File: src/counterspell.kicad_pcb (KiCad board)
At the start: 2 copper layers, 50.7 x 116.8 mm, 10 parts, among them SW1 SW_Push

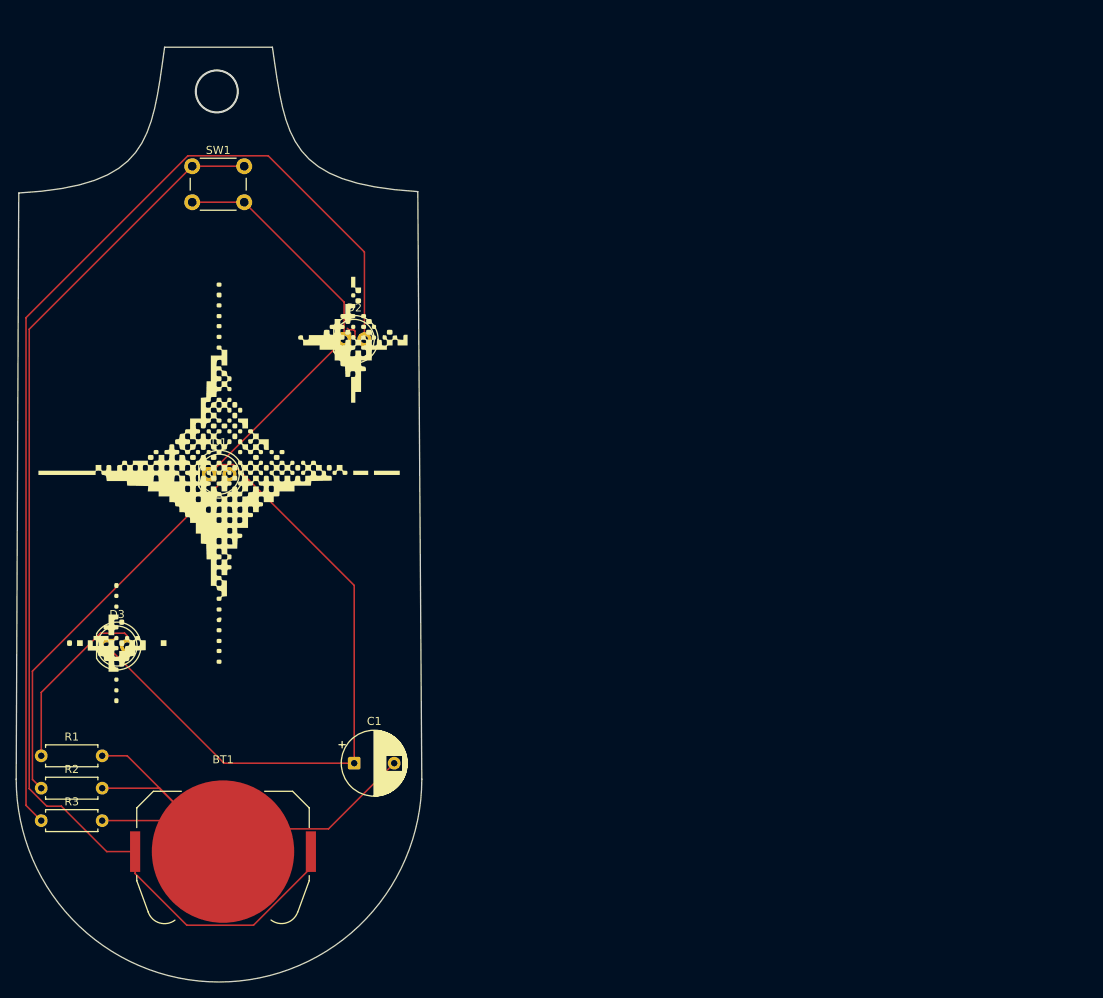
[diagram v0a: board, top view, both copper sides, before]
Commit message: perfect changed the whole board outlook like resized it
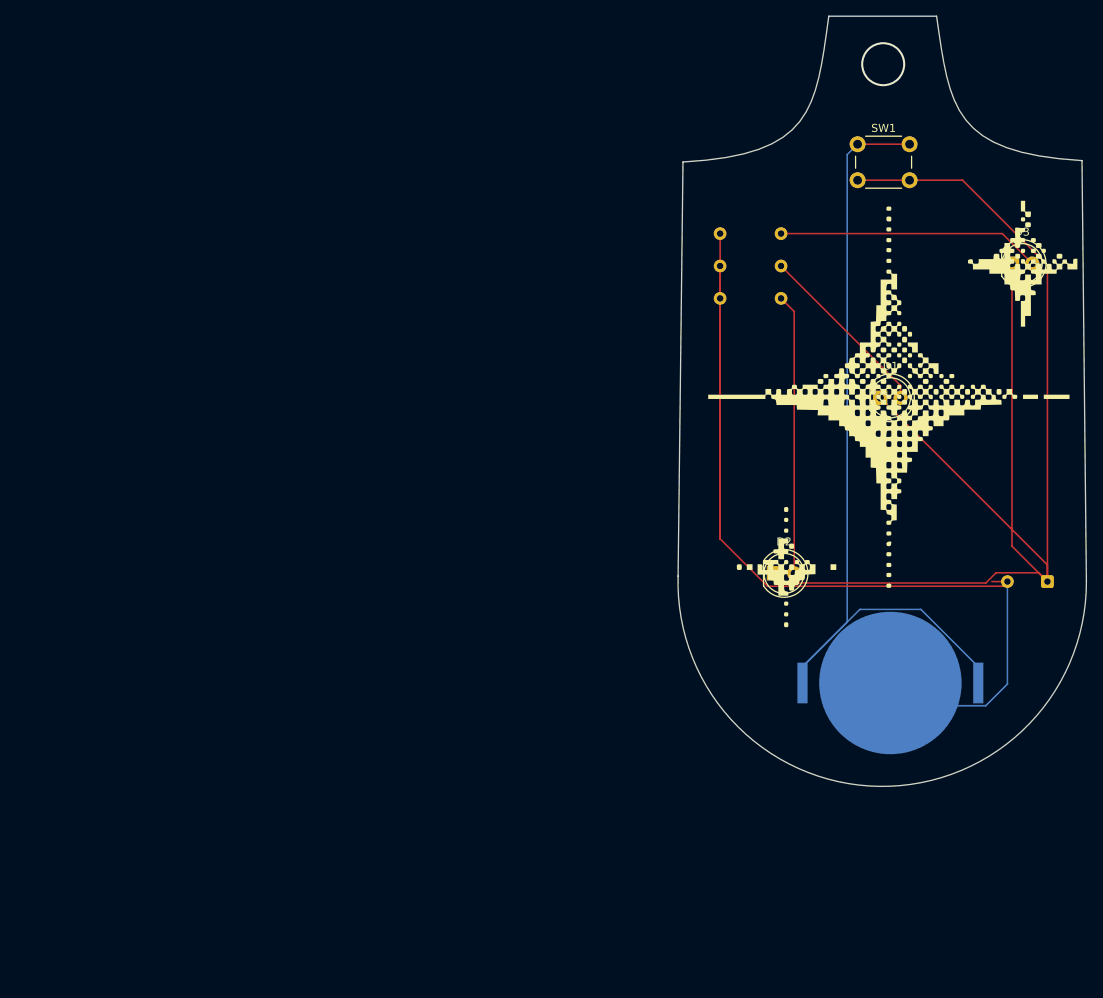
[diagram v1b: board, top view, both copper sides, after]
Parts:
- BT1, C1, R1, R2, R3: moved to B.Cu
- moved D3 122.8 mm to (249.8, 56.3)
- moved R1 113.2 mm to (220.9, 52.5), turned to 180 degrees
- moved R2 113.2 mm to (220.9, 56.6), turned to 180 degrees
- moved R3 113.2 mm to (220.9, 60.6), turned to 180 degrees
- moved C1 89.6 mm to (254.2, 96.0), turned to 180 degrees
- moved BT1 86.0 mm to (234.6, 108.7), turned to 180 degrees
- moved D1 84.4 mm to (233.3, 73.1)
- moved G*** 84.3 mm to (234.9, 75.1)
- moved SW1 83.2 mm to (230.5, 41.4)
- moved D2 61.2 mm to (220.0, 95.0)
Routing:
- net Net-(D2-A): track 130.2 -> 35.1 mm
- net Net-(BT1--): track 81.1 -> 172.6 mm
- net Net-(D1-K): track 138.5 -> 176.6 mm
- net Net-(BT1-+): track 141.6 -> 106.6 mm
- net Net-(D1-A): track 49.9 -> 22.7 mm
- net Net-(D3-A): track 23.1 -> 33.0 mm
- net (no net): track 1.87 -> 0.00 mm
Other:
- board size 50.7 x 116.8 mm -> 51 x 96.3 mm

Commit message: Update counterspell.kicad_pcb
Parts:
- added G***: LOGO, LOGO, B.Cu at (252.1, 81.3)
- added G***: LOGO, LOGO, B.Cu at (242.6, 75.6)

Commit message: important
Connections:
- C1 pad 1: Net-(D1-K) -> Net-(D1-A)
- D2 pad 1: Net-(D1-K) -> Net-(D2-K)
- D2 pad 2: Net-(D2-A) -> Net-(D1-A)
- D3 pad 1: Net-(D1-K) -> Net-(D3-K)
- D3 pad 2: Net-(D3-A) -> Net-(D1-A)
- R1 pad 1: Net-(D3-A) -> Net-(D3-K)
- R2 pad 1: Net-(D1-A) -> Net-(D1-K)
- R3 pad 1: Net-(D2-A) -> Net-(D2-K)
- SW1 pad 2: Net-(D1-K) -> Net-(D1-A)
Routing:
- net Net-(D1-K): track 176.6 -> 21.6 mm
- net Net-(D1-A): track 22.7 -> 107.8 mm
- net Net-(BT1--): track 172.6 -> 106.2 mm
- net Net-(D2-A): track 35.1 -> 0.00 mm
- net Net-(D2-K): track 0.00 -> 34.7 mm
- net Net-(D3-A): track 33.0 -> 0.00 mm
- net Net-(D3-K): track 0.00 -> 30.4 mm
- net Net-(BT1-+): track 106.6 -> 105.3 mm
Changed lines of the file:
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@@
 	(net 3 "Net-(D1-K)")
 	(net 4 "Net-(D1-A)")
-	(net 5 "Net-(D2-A)")
-	(net 6 "Net-(D3-A)")
+	(net 5 "Net-(D2-K)")
+	(net 6 "Net-(D3-K)")
 	(footprint "LED_THT:LED_D5.0mm"
 		(layer "F.Cu")
@@
 			(layers "*.Cu" "*.Mask")
 			(remove_unused_layers no)
-			(net 3 "Net-(D1-K)")
+			(net 6 "Net-(D3-K)")
 			(pinfunction "K")
 			(pintype "passive")
@@
 			(layers "*.Cu" "*.Mask")
 			(remove_unused_layers no)
-			(net 6 "Net-(D3-A)")
+			(net 4 "Net-(D1-A)")
 			(pinfunction "A")
 			(pintype "passive")
@@
 			(layers "*.Cu" "*.Mask")
 			(remove_unused_layers no)
-			(net 3 "Net-(D1-K)")
+			(net 5 "Net-(D2-K)")
 			(pinfunction "K")
 			(pintype "passive")
@@
 			(layers "*.Cu" "*.Mask")
 			(remove_unused_layers no)
-			(net 5 "Net-(D2-A)")
+			(net 4 "Net-(D1-A)")
 			(pinfunction "A")
 			(pintype "passive")
@@
 			(layers "*.Cu" "*.Mask")
 			(remove_unused_layers no)
-			(net 3 "Net-(D1-K)")
+			(net 4 "Net-(D1-A)")
 			(pinfunction "2")
 			(pintype "passive")
@@
 			(layers "*.Cu" "*.Mask")
 			(remove_unused_layers no)
-			(net 3 "Net-(D1-K)")
+			(net 4 "Net-(D1-A)")
 			(pinfunction "2")
 			(pintype "passive")
@@
 			(remove_unused_layers no)
 			(roundrect_rratio 0.15625)
-			(net 3 "Net-(D1-K)")
+			(net 4 "Net-(D1-A)")
 			(pintype "passive")
 		)
@@
 			(layers "*.Cu" "*.Mask")
 			(remove_unused_layers no)
-			(net 4 "Net-(D1-A)")
+			(net 3 "Net-(D1-K)")
 			(pintype "passive")
 		)
@@
 			(layers "*.Cu" "*.Mask")
 			(remove_unused_layers no)
-			(net 5 "Net-(D2-A)")
+			(net 5 "Net-(D2-K)")
 			(pintype "passive")
 		)
@@
 			(layers "*.Cu" "*.Mask")
 			(remove_unused_layers no)
-			(net 6 "Net-(D3-A)")
+			(net 6 "Net-(D3-K)")
 			(pintype "passive")
 		)
@@
 	)
 	(segment
-		(start 248.650651 96.627)
-		(end 249.227651 96.05)
-		(width 0.2)
-		(layer "F.Cu")
-		(net 1)
-	)
-	(segment
 		(start 213.315 90.707)
-		(end 219.235 96.627)
+		(end 218.834 96.226)
 		(width 0.2)
 		(layer "F.Cu")
@@
 	)
 	(segment
-		(start 213.315 52.55)
-		(end 213.315 90.707)
+		(start 249.051651 96.226)
+		(end 249.227651 96.05)
 		(width 0.2)
 		(layer "F.Cu")
@@
 	)
 	(segment
-		(start 219.235 96.627)
-		(end 248.650651 96.627)
+		(start 218.834 96.226)
+		(end 249.051651 96.226)
 		(width 0.2)
 		(layer "F.Cu")
@@
 	)
 	(segment
-		(start 247.275 96.05)
-		(end 249.227651 96.05)
+		(start 213.315 52.55)
+		(end 213.315 56.6)
 		(width 0.2)
 		(layer "F.Cu")
@@
 	(segment
 		(start 213.315 56.6)
-		(end 213.315 90.707)
+		(end 213.315 60.65)
 		(width 0.2)
 		(layer "F.Cu")
@@
 	)
 	(segment
-		(start 249.227651 108.859349)
-		(end 249.227651 96.05)
+		(start 237.441 111.566)
+		(end 246.521 111.566)
 		(width 0.2)
 		(layer "B.Cu")
@@
 	)
 	(segment
-		(start 237.441 111.566)
-		(end 246.521 111.566)
+		(start 249.227651 108.859349)
+		(end 249.227651 96.05)
 		(width 0.2)
 		(layer "B.Cu")
@@
 	)
 	(segment
-		(start 229.199 42.676)
-		(end 230.5 41.375)
-		(width 0.2)
-		(layer "B.Cu")
-		(net 2)
-	)
-	(segment
-		(start 223.615 108.725)
-		(end 223.615 106.697821)
-		(width 0.2)
-		(layer "B.Cu")
-		(net 2)
-	)
-	(segment
-		(start 229.199 101.113821)
-		(end 229.199 42.676)
+		(start 245.585 49.96)
+		(end 237 41.375)
 		(width 0.2)
 		(layer "B.Cu")
@@
 	)
 	(segment
-		(start 223.615 106.697821)
-		(end 229.199 101.113821)
+		(start 245.585 108.725)
+		(end 245.585 49.96)
 		(width 0.2)
 		(layer "B.Cu")
@@
 	)
 	(segment
-		(start 245.585 106.697821)
-		(end 245.585 108.725)
-		(width 0.2)
-		(layer "B.Cu")
-		(net 2)
-	)
-	(segment
-		(start 237 45.875)
-		(end 243.613471 45.875)
-		(width 0.2)
-		(layer "F.Cu")
-		(net 3)
-	)
-	(segment
-		(start 220.035 95.025)
-		(end 221.236 96.226)
-		(width 0.2)
-		(layer "F.Cu")
-		(net 3)
-	)
-	(segment
-		(start 247.8089 94.949)
-		(end 253.126651 94.949)
-		(width 0.2)
-		(layer "F.Cu")
-		(net 3)
-	)
-	(segment
-		(start 243.613471 45.875)
-		(end 254.227651 56.48918)
-		(width 0.2)
-		(layer "F.Cu")
-		(net 3)
-	)
-	(segment
-		(start 230.5 45.875)
-		(end 237 45.875)
+		(start 220.935 56.6)
+		(end 233.335 69)
 		(width 0.2)
 		(layer "F.Cu")
@@
 	)
 	(segment
-		(start 254.227651 93.967651)
+		(start 233.335 69)
 		(end 233.335 73.075)
 		(width 0.2)
@@
 	)
 	(segment
-		(start 249.8 56.3)
-		(end 249.8 91.622349)
+		(start 252.34 56.61)
+		(end 252.34 56.3)
 		(width 0.2)
 		(layer "F.Cu")
-		(net 3)
+		(net 4)
 	)
 	(segment
-		(start 221.236 96.226)
-		(end 246.5319 96.226)
+		(start 222.575 86.375)
+		(end 235.875 73.075)
 		(width 0.2)
 		(layer "F.Cu")
-		(net 3)
+		(net 4)
 	)
 	(segment
-		(start 249.8 91.622349)
-		(end 254.227651 96.05)
+		(start 235.875 73.075)
+		(end 252.34 56.61)
 		(width 0.2)
 		(layer "F.Cu")
-		(net 3)
+		(net 4)
 	)
 	(segment
-		(start 253.126651 94.949)
-		(end 254.227651 96.05)
+		(start 241.915 45.875)
+		(end 252.34 56.3)
 		(width 0.2)
 		(layer "F.Cu")
-		(net 3)
+		(net 4)
 	)
 	(segment
-		(start 254.227651 96.05)
-		(end 254.227651 93.967651)
+		(start 237 45.875)
+		(end 241.915 45.875)
 		(width 0.2)
 		(layer "F.Cu")
-		(net 3)
+		(net 4)
 	)
 	(segment
-		(start 246.5319 96.226)
-		(end 247.8089 94.949)
+		(start 235.875 73.075)
+		(end 235.875 77.697349)
 		(width 0.2)
 		(layer "F.Cu")
-		(net 3)
+		(net 4)
 	)
 	(segment
-		(start 254.227651 56.48918)
+		(start 235.875 77.697349)
 		(end 254.227651 96.05)
 		(width 0.2)
 		(layer "F.Cu")
-		(net 3)
+		(net 4)
 	)
 	(segment
-		(start 235.875 73.075)
-		(end 235.875 71.54)
+		(start 222.575 95.025)
+		(end 222.575 86.375)
 		(width 0.2)
 		(layer "F.Cu")
@@
 	)
 	(segment
-		(start 235.875 71.54)
-		(end 220.935 56.6)
+		(start 230.5 45.875)
+		(end 237 45.875)
 		(width 0.2)
 		(layer "F.Cu")
@@
 	)
 	(segment
-		(start 222.575 95.025)
-		(end 222.575 62.29)
+		(start 220.935 60.65)
+		(end 220.935 94.125)
 		(width 0.2)
 		(layer "F.Cu")
@@
 	)
 	(segment
-		(start 222.575 62.29)
-		(end 220.935 60.65)
+		(start 220.935 94.125)
+		(end 220.035 95.025)
 		(width 0.2)
 		(layer "F.Cu")
@@
 	)
 	(segment
-		(start 248.59 52.55)
-		(end 220.935 52.55)
+		(start 220.935 52.55)
+		(end 246.05 52.55)
 		(width 0.2)
 		(layer "F.Cu")
@@
 	)
 	(segment
-		(start 252.34 56.3)
-		(end 248.59 52.55)
+		(start 246.05 52.55)
+		(end 249.8 56.3)
 		(width 0.2)
 		(layer "F.Cu")

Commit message: important stuff
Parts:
- moved D2 52.4 mm to (249.2, 51.5)
- moved D3 45.6 mm to (218.9, 89.8)
- moved C1 34.3 mm to (225.3, 77.6)
- moved BT1 12.5 mm to (235.9, 96.3)
- moved R2 6.70 mm to (220.3, 49.9)
- moved R1 6.70 mm to (220.3, 45.9)
- moved R3 6.70 mm to (220.3, 54.0)
- moved D1 5.68 mm to (232.2, 67.5)
- moved G*** 4.98 mm to (250.8, 76.5)
- moved G*** 4.98 mm to (241.3, 70.8)
- moved G*** 4.98 mm to (233.6, 70.3)
- moved SW1 1.78 mm to (230.6, 39.6)
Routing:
- net Net-(BT1--): track 106.2 -> 71.0 mm
- net Net-(D1-A): track 107.8 -> 77.4 mm
- net Net-(D3-K): track 30.4 -> 46.2 mm
- net Net-(D1-K): track 21.6 -> 34.2 mm
- net Net-(D2-K): track 34.7 -> 43.0 mm
- net Net-(BT1-+): track 105.3 -> 97.5 mm
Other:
- board size 51 x 96.3 mm -> 47 x 83.4 mm
